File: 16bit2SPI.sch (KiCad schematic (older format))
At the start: 5 parts, among them J3 TFT, U3 74HC04, U4 74HC4094, U5 74HC4094, U6 74HC4040

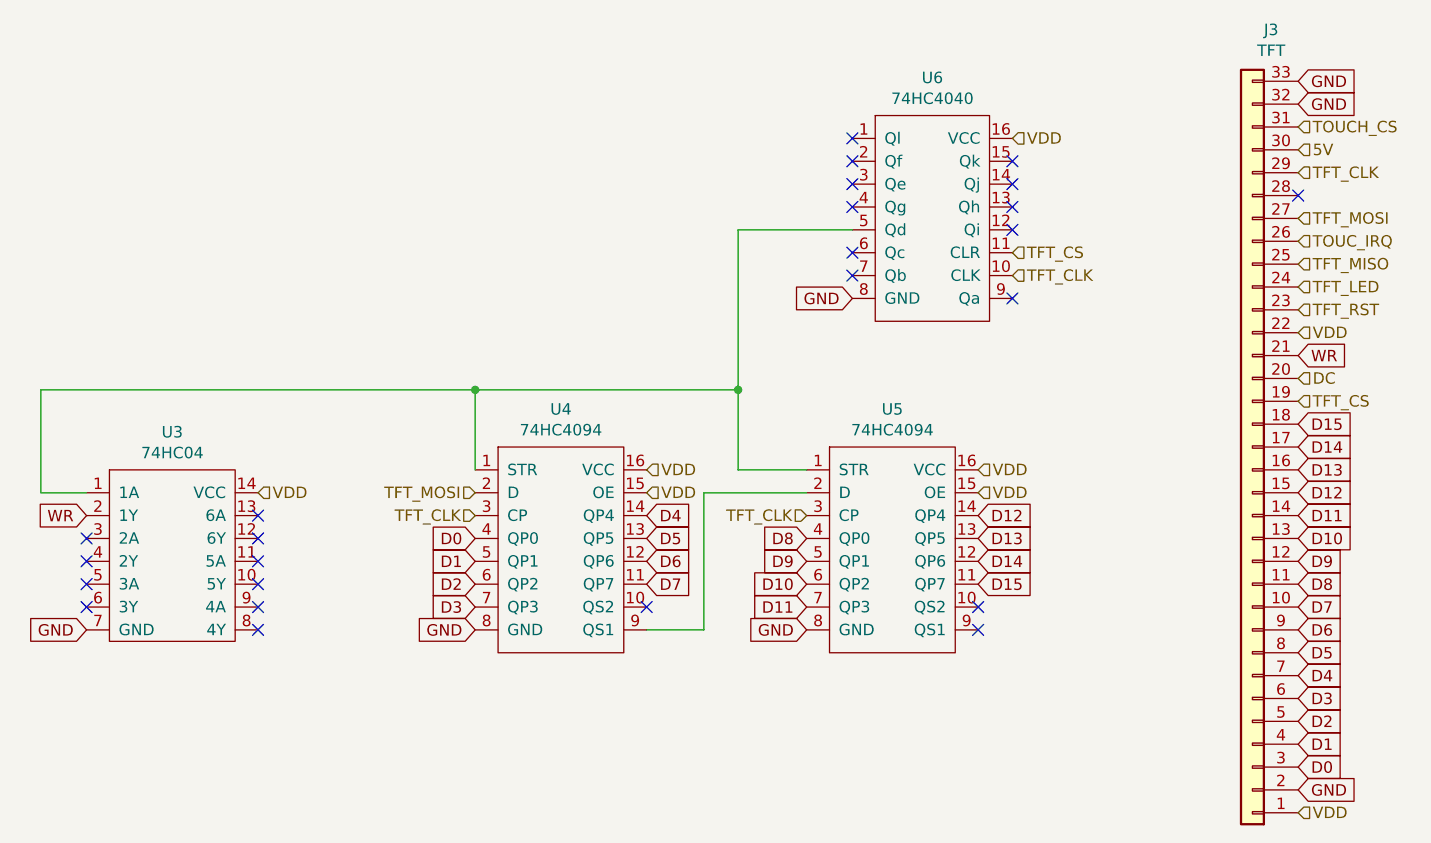
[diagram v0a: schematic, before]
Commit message: Разъем под акселерометр Блок. конденсаторы Управление подстветкой экрана
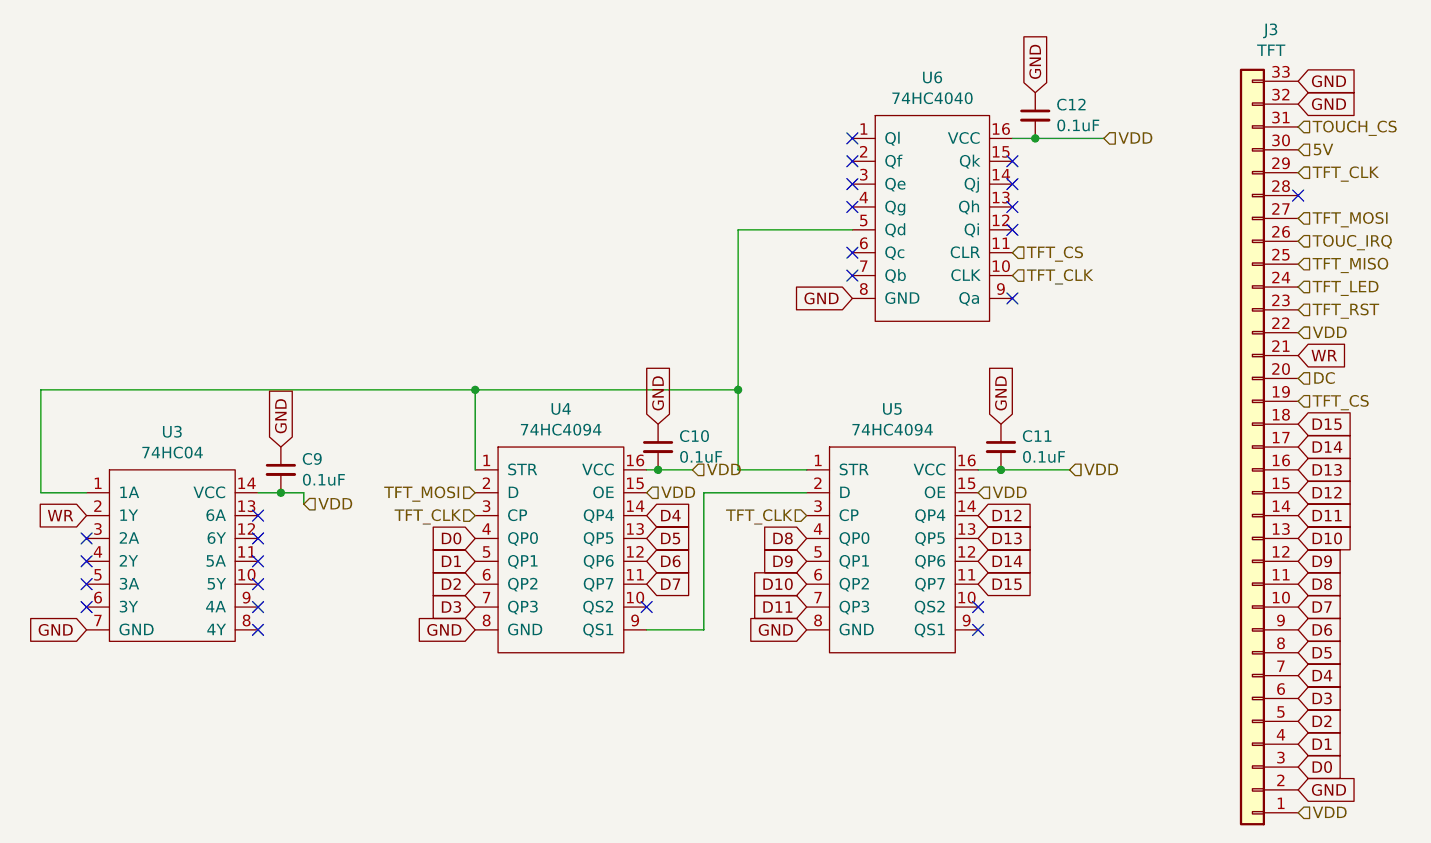
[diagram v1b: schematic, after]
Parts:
- added C10, C11, C12, C9: 0.1uF, Capacitor_SMD:C_0805_2012Metric, symbol Device:C_Small
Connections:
- net GND: now also C10.1, C11.1, C12.1, C9.1
- net VDD: now also C10.2, C11.2, C12.2, C9.2
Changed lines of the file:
@@
 	1    0    0    -1
 $EndComp
-Text HLabel 5000 2750 2    50   Input ~ 0
-VDD
-Text HLabel 6600 1300 2    50   Input ~ 0
-VDD
-Text HLabel 3300 2850 2    50   Input ~ 0
-VDD
-Text HLabel 6450 2750 2    50   Input ~ 0
+Text HLabel 5200 2750 2    50   Input ~ 0
+VDD
+Text HLabel 7000 1300 2    50   Input ~ 0
+VDD
+Text HLabel 3500 2900 2    50   Input ~ 0
+VDD
+Text HLabel 6850 2750 2    50   Input ~ 0
 VDD
 Wire Wire Line
@@
 Text HLabel 7850 4250 2    50   Input ~ 0
 VDD
+$Comp
+L Device:C_Small C12
+U 1 1 616FF85C
+P 6700 1200
+F 0 "C12" H 6792 1246 50  0000 L CNN
+F 1 "0.1uF" H 6792 1155 50  0000 L CNN
+F 2 "Capacitor_SMD:C_0805_2012Metric" H 6700 1200 50  0001 C CNN
+F 3 "~" H 6700 1200 50  0001 C CNN
+	1    6700 1200
+	1    0    0    -1
+$EndComp
+Wire Wire Line
+	6600 1300 6700 1300
+Wire Wire Line
+	7000 1300 6700 1300
+Connection ~ 6700 1300
+Text GLabel 6700 1100 1    50   Input ~ 0
+GND
+$Comp
+L Device:C_Small C11
+U 1 1 61703D98
+P 6550 2650
+F 0 "C11" H 6642 2696 50  0000 L CNN
+F 1 "0.1uF" H 6642 2605 50  0000 L CNN
+F 2 "Capacitor_SMD:C_0805_2012Metric" H 6550 2650 50  0001 C CNN
+F 3 "~" H 6550 2650 50  0001 C CNN
+	1    6550 2650
+	1    0    0    -1
+$EndComp
+Wire Wire Line
+	6450 2750 6550 2750
+Wire Wire Line
+	6550 2750 6850 2750
+Connection ~ 6550 2750
+Text GLabel 6550 2550 1    50   Input ~ 0
+GND
+$Comp
+L Device:C_Small C10
+U 1 1 6170AC3B
+P 5050 2650
+F 0 "C10" H 5142 2696 50  0000 L CNN
+F 1 "0.1uF" H 5142 2605 50  0000 L CNN
+F 2 "Capacitor_SMD:C_0805_2012Metric" H 5050 2650 50  0001 C CNN
+F 3 "~" H 5050 2650 50  0001 C CNN
+	1    5050 2650
+	1    0    0    -1
+$EndComp
+Text GLabel 5050 2550 1    50   Input ~ 0
+GND
+Wire Wire Line
+	5000 2750 5050 2750
+Connection ~ 5050 2750
+Wire Wire Line
+	5050 2750 5200 2750
+$Comp
+L Device:C_Small C9
+U 1 1 617108B6
+P 3400 2750
+F 0 "C9" H 3492 2796 50  0000 L CNN
+F 1 "0.1uF" H 3492 2705 50  0000 L CNN
+F 2 "Capacitor_SMD:C_0805_2012Metric" H 3400 2750 50  0001 C CNN
+F 3 "~" H 3400 2750 50  0001 C CNN
+	1    3400 2750
+	1    0    0    -1
+$EndComp
+Wire Wire Line
+	3300 2850 3400 2850
+Wire Wire Line
+	3400 2850 3500 2850
+Wire Wire Line
+	3500 2850 3500 2900
+Connection ~ 3400 2850
+Text GLabel 3400 2650 1    50   Input ~ 0
+GND
 $EndSCHEMATC

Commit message: v2
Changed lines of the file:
@@
 Text HLabel 7000 1300 2    50   Input ~ 0
 VDD
-Text HLabel 3500 2900 2    50   Input ~ 0
+Text HLabel 3500 2850 2    50   Input ~ 0
 VDD
 Text HLabel 6850 2750 2    50   Input ~ 0
@@
 GND
 Wire Wire Line
-	5700 2750 5400 2750
-Wire Wire Line
-	5400 2750 5400 2400
+	5700 2750 5600 2750
 Wire Wire Line
 	5400 1700 5900 1700
@@
 	4250 2400 5400 2400
 Connection ~ 4250 2400
-Connection ~ 5400 2400
 Wire Wire Line
 	5400 2400 5400 1700
@@
 U 1 1 617108B6
 P 3400 2750
-F 0 "C9" H 3492 2796 50  0000 L CNN
-F 1 "0.1uF" H 3492 2705 50  0000 L CNN
+F 0 "C9" H 3500 2900 50  0000 L CNN
+F 1 "0.1uF" H 3500 2800 50  0000 L CNN
 F 2 "Capacitor_SMD:C_0805_2012Metric" H 3400 2750 50  0001 C CNN
 F 3 "~" H 3400 2750 50  0001 C CNN
@@
 Wire Wire Line
 	3400 2850 3500 2850
-Wire Wire Line
-	3500 2850 3500 2900
 Connection ~ 3400 2850
 Text GLabel 3400 2650 1    50   Input ~ 0
 GND
+Wire Wire Line
+	5400 2400 5600 2400
+Wire Wire Line
+	5600 2400 5600 2750
+Connection ~ 5400 2400
 $EndSCHEMATC
